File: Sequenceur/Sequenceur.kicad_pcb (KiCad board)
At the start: 4 copper layers, 78.7 x 121.9 mm, 49 parts, among them J1 AudioJack2, J2 Jack-DC, SW1 SW_Push, SW2 SW_Rotary12, U1 NE555P, U2 4017, U3 OP07

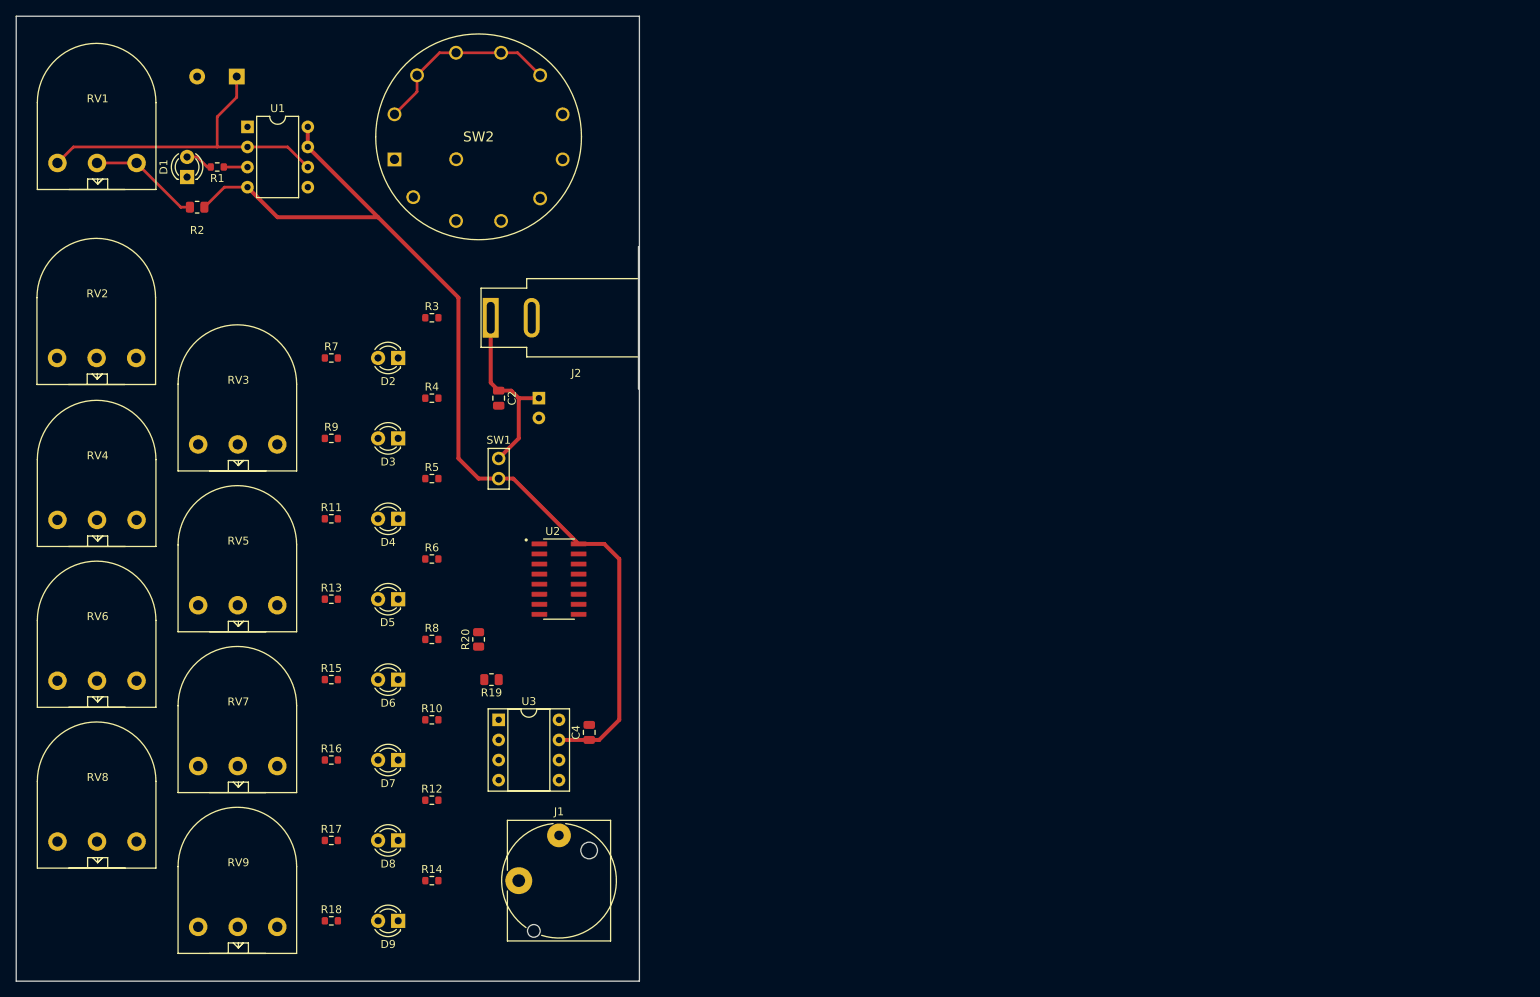
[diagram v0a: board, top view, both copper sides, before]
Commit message: First real version of the PCB, as a 2 layer one, and with adapted footprints.
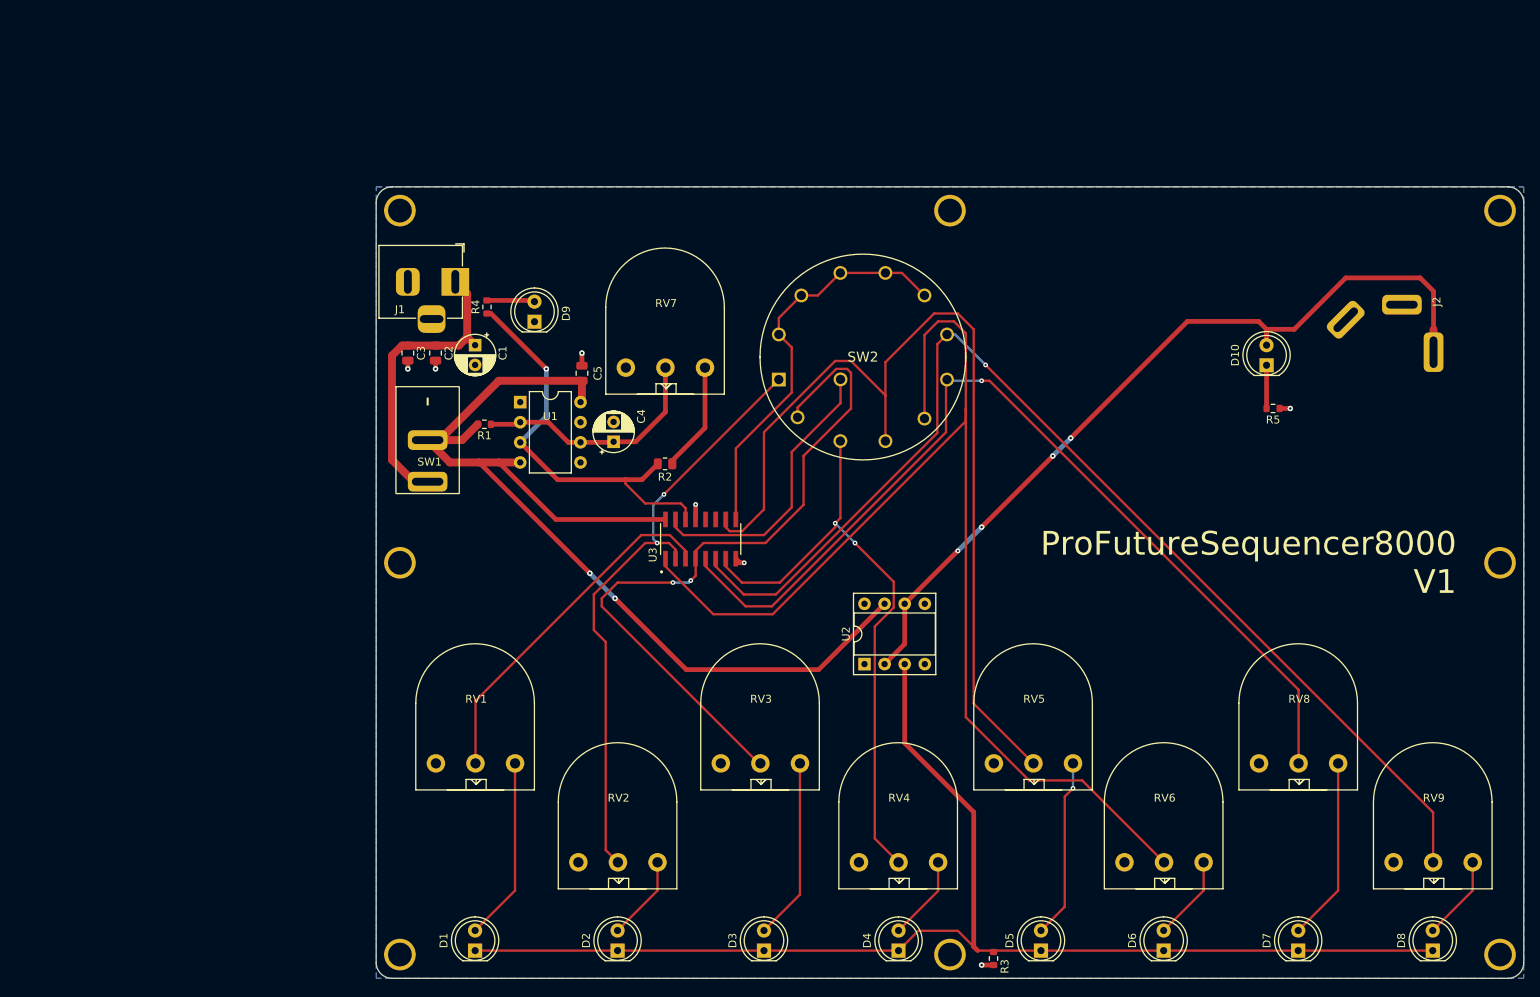
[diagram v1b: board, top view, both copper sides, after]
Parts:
- removed R10, R12, R14, R6, R8: 100R, Resistor_SMD:R_0603_1608Metric
- removed R11, R13, R15, R16, R17, R18, R7, R9: 1K, Resistor_SMD:R_0603_1608Metric
- removed R19: 470R, Resistor_SMD:R_0805_2012Metric
- removed R20: 300R, Resistor_SMD:R_0805_2012Metric
- added ?: , , F.Cu at (220.5, 52.5)
- added ?: , , F.Cu at (81.5, 146.5)
- added ?: , , F.Cu at (220.5, 146.5)
- added ?: , , F.Cu at (220.5, 97.0)
- added ?: , , F.Cu at (151.0, 146.5)
- added ?: , , F.Cu at (81.5, 97.0)
- added ?: , , F.Cu at (151.0, 52.5)
- added ?: , , F.Cu at (81.5, 52.5)
- added C5: .1u, Capacitor_SMD:C_0805_2012Metric, F.Cu at (104.5, 73.0)
- added D10: 2V, 10mA, LED_THT:LED_D5.0mm, F.Cu at (191.0, 72.0)
- C1: moved to F.Cu
- C3: value 680u -> 1u; footprint Capacitor_THT:CP_Radial_D10.0mm_P5.00mm -> Capacitor_SMD:C_0805_2012Metric; moved to F.Cu
- C4: value .1u -> 22u; footprint Capacitor_SMD:C_0805_2012Metric -> Capacitor_THT:CP_Radial_D5.0mm_P2.50mm
- D1: value LED -> 2V, 10mA; footprint LED_THT:LED_D3.0mm -> LED_THT:LED_D5.0mm
- D2, D3, D4, D5, D6, D7, D8, D9: footprint LED_THT:LED_D3.0mm -> LED_THT:LED_D5.0mm
- J1: value AudioJack2 -> Jack-DC; footprint Connector_Audio:Jack_6.35mm_Neutrik_NJ2FD-V_Vertical -> Connector_BarrelJack:BarrelJack_Horizontal
- J2: value Jack-DC -> AudioJack2_SwitchT; footprint Connector_BarrelJack:BarrelJack_SwitchcraftConxall_RAPC10U_Horizontal -> User_added:Jack_6.35_TTnS
- R1: value 1K -> 100K
- R3: value 100R -> 100K
- R4, R5: value 100R -> 1K
- SW1: footprint User_added:PAD_2_std -> User_added:Switch_2pin
- U2: value 4017 -> OP07; footprint User_added:CD4017BM -> User_added:DIP-8
- U3: value OP07 -> 4017; footprint User_added:DIP-8 -> User_added:CD4017BM
- moved RV8 152.1 mm to (190.0, 122.3)
- moved RV9 151.3 mm to (207.0, 134.8)
- moved RV6 136.8 mm to (173.0, 134.8)
- moved D8 131.5 mm to (212.0, 146.0), turned to 90 degrees
- moved D7 116.2 mm to (195.0, 146.0), turned to 90 degrees
- moved RV4 110.1 mm to (139.5, 134.8)
- moved R3 107.7 mm to (156.5, 147.0), turned to -90 degrees
- moved R5 106.7 mm to (191.8, 77.5), turned to 180 degrees
- moved J2 105.5 mm to (197.7, 78.8), turned to 0 degrees
- moved D1 104.3 mm to (91.0, 146.0)
- moved D6 102.6 mm to (178.0, 146.0), turned to 90 degrees
- moved RV5 102.5 mm to (156.5, 122.3)
- moved D5 92.6 mm to (162.5, 146.0), turned to 90 degrees
- moved RV2 91.6 mm to (104.0, 134.8)
- moved RV1 89.7 mm to (86.0, 122.3)
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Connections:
- C3 pad 1: Net-(U1-THR) -> Net-(C1-Pad1)
- C4 pad 1: VCC -> Net-(U1-THR)
- D1 pad 1: GND -> Net-(D1-K)
- D2 pad 1: GND -> Net-(D1-K)
- D3 pad 1: GND -> Net-(D1-K)
- D4 pad 1: GND -> Net-(D1-K)
- D5 pad 1: GND -> Net-(D1-K)
- D6 pad 1: GND -> Net-(D1-K)
- D7 pad 1: GND -> Net-(D1-K)
- D8 pad 1: GND -> Net-(D1-K)
- R1 pad 1: Net-(U1-Q) -> Net-(U1-THR)
- R1 pad 2: Net-(D1-A) -> VCC
- R2 pad 1: VCC -> Net-(R2-Pad1)
- R2 pad 2: Net-(R2-Pad2) -> Net-(U1-Q)
- R3 pad 1: Net-(R3-Pad1) -> Net-(D1-K)
- R3 pad 2: Net-(U3-+) -> GND
- R4 pad 1: Net-(R4-Pad1) -> Net-(U1-Q)
- R4 pad 2: Net-(U3-+) -> Net-(D9-A)
- R5 pad 1: Net-(R11-Pad1) -> GND
- R5 pad 2: Net-(U3-+) -> Net-(D10-K)
- RV1 pad 1: Net-(U1-THR) -> GND
- RV1 pad 2: Net-(R2-Pad2) -> sig_0
- RV1 pad 3: Net-(R2-Pad2) -> Net-(D1-A)
- RV2 pad 2: Net-(R3-Pad1) -> sig_1
- RV2 pad 3: sig_0 -> Net-(D2-A)
- RV3 pad 2: Net-(R4-Pad1) -> sig_2
- RV3 pad 3: sig_1 -> Net-(D3-A)
- RV4 pad 2: Net-(R11-Pad1) -> sig_3
- RV4 pad 3: sig_2 -> Net-(D4-A)
- RV5 pad 2: Net-(R13-Pad1) -> sig_4
- RV5 pad 3: sig_3 -> Net-(D5-A)
- RV6 pad 2: Net-(R15-Pad1) -> sig_5
- RV6 pad 3: sig_4 -> Net-(D6-A)
- RV7 pad 1: GND -> unconnected-(RV7-Pad1)
- RV7 pad 2: Net-(R10-Pad1) -> Net-(U1-THR)
- RV7 pad 3: sig_5 -> Net-(R2-Pad1)
- RV8 pad 2: Net-(R12-Pad1) -> sig_6
- RV8 pad 3: sig_6 -> Net-(D7-A)
- RV9 pad 2: Net-(R14-Pad1) -> sig_7
- RV9 pad 3: sig_7 -> Net-(D8-A)
- SW2 pad 10: Net-(U2-Q8) -> Net-(U3-Q8)
- SW2 pad 11: Net-(U2-Q8) -> Net-(U3-Q8)
- SW2 pad 12: Net-(U2-Q8) -> Net-(U3-Q8)
- SW2 pad 13: Net-(U2-Reset) -> Net-(U3-Reset)
- SW2 pad 8: Net-(U2-Q8) -> Net-(U3-Q8)
- SW2 pad 9: Net-(U2-Q8) -> Net-(U3-Q8)
- U1 pad 7: VCC -> unconnected-(U1-DIS-Pad7)
- U2 pad 1: sig_5 -> unconnected-(U2-VOS-Pad1)
- U2 pad 2: sig_1 -> Net-(D10-A)
- U2 pad 3: sig_0 -> Net-(D1-K)
- U2 pad 4: sig_2 -> GND
- U2 pad 5: sig_6 -> unconnected-(U2-NC-Pad5)
- U2 pad 6: sig_7 -> Net-(D10-A)
- U2 pad 7: sig_3 -> VCC
- U2 pad 8: GND -> unconnected-(U2-VOS-Pad8)
- U3 pad 1: GND -> sig_5
- U3 pad 2: Net-(U3--) -> sig_1
- U3 pad 3: Net-(U3-+) -> sig_0
- U3 pad 4: GND -> sig_2
- U3 pad 5: unconnected-(U3-NC-Pad5) -> sig_6
- U3 pad 6: Net-(J1-PadT) -> sig_7
- U3 pad 7: VCC -> sig_3
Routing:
- net Net-(D1-K): track 0.00 -> 162.4 mm
- net sig_5: track 0.00 -> 151.4 mm
- net sig_7: track 0.00 -> 144.6 mm, vias 0 -> 1
- net sig_4: track 0.00 -> 120.2 mm
- net sig_6: track 0.00 -> 118.8 mm, vias 0 -> 1
- net Net-(D10-A): track 0.00 -> 103.8 mm, vias 0 -> 4
- net sig_2: track 0.00 -> 91.0 mm, vias 0 -> 2
- net sig_3: track 0.00 -> 77.8 mm, vias 0 -> 2
- net sig_1: track 0.00 -> 77.0 mm, vias 0 -> 2
- net Net-(U3-Q8): track 0.00 -> 51.0 mm
- net Net-(U1-Q): track 3.00 -> 52.0 mm, vias 0 -> 1
- net sig_0: track 0.00 -> 44.9 mm
- net Net-(U3-Reset): track 0.00 -> 36.2 mm
- net Net-(U2-Q8): track 24.0 -> 0.00 mm
- net Net-(D7-A): track 0.00 -> 23.2 mm
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- added copper zone on B.Cu, net GND
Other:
- board size 78.7 x 121.9 mm -> 145 x 100 mm
- copper layers 4 -> 2
- board text added: "ProFutureSequencer8000 V1"
- board text added: "WayWayWay"
